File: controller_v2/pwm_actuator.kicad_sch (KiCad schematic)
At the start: 22 parts, among them J1 Conn_01x03_Socket, J2 WAGO 236-402, J3 WAGO 236-402, J4 WAGO 236-404, Q1 2N2222

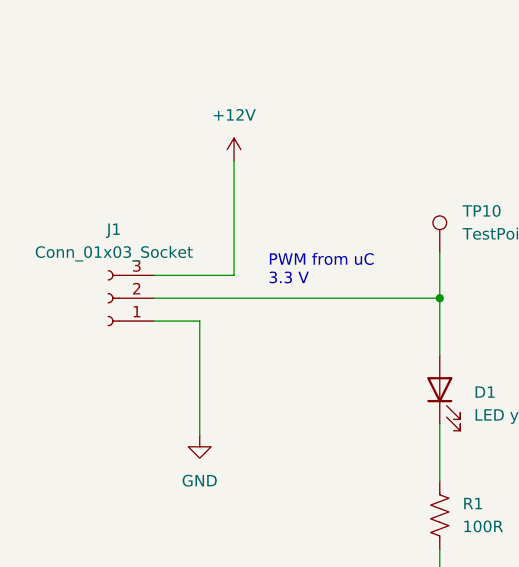
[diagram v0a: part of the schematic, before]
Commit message: Replaced symbols with custom print connector
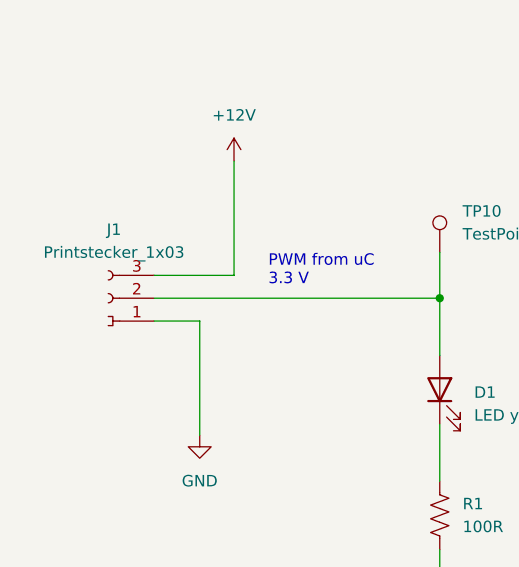
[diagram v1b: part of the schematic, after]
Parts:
- removed J1: Conn_01x03_Socket, Connector_PinSocket_2.54mm:PinSocket_1x03_P2.54mm_Vertical, symbol Connector:Conn_01x03_Socket
- added J1: Printstecker_1x03, connectors:printstecker_1x03_P2.54mm, symbol connectors:printstecker_1x03
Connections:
- net +12V: now also J1.3 (Pin_3)
- net GND: now also J1.1 (Pin_1)
- net at D1.2 (A), TP10.1: now also J1.2 (Pin_2)
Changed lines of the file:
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@@
-    )
-  )
-  (symbol (lib_id "Connector:Conn_01x03_Socket") (at 41.91 88.9 180) (unit 1)
-    (in_bom yes) (on_board yes) (dnp no) (fields_autoplaced)
-    (property "Reference" "J1" (at 42.545 81.28 0)
-      (effects (font (size 1.27 1.27)))
-    )
-    (property "Value" "Conn_01x03_Socket" (at 42.545 83.82 0)
-      (effects (font (size 1.27 1.27)))
-    )
-    (property "Footprint" "Connector_PinSocket_2.54mm:PinSocket_1x03_P2.54mm_Vertical" (at 41.91 88.9 0)
-      (effects (font (size 1.27 1.27)) hide)
-    )
-    (property "Datasheet" "~" (at 41.91 88.9 0)
-      (effects (font (size 1.27 1.27)) hide)
-    )
-    (pin "1")
-    (pin "2")
-    (pin "3")
-    (instances
-      (project "controller"
-        (path "/12246f82-5c9a-456f-a9a1-28ea473855be"
-          (reference "J1") (unit 1)
-        )
-      )
-      (project "controller_v2"
-        (path "/884d8f78-75d7-4449-b027-2ba1bd4eeac8"
-          (reference "J?") (unit 1)
-        )
-        (path "/884d8f78-75d7-4449-b027-2ba1bd4eeac8/e6f5d033-74f5-43d5-8e72-d0169a25c706"
-          (reference "J1") (unit 1)
-        )
-      )
     )
   )
@@
         )
       )
+    )
+  )
+  (symbol (lib_id "connectors:printstecker_1x03") (at 41.91 88.9 180) (unit 1)
+    (in_bom yes) (on_board yes) (dnp no) (fields_autoplaced)
+    (property "Reference" "J1" (at 42.545 81.28 0)
+      (effects (font (size 1.27 1.27)))
+    )
+    (property "Value" "Printstecker_1x03" (at 42.545 83.82 0)
+      (effects (font (size 1.27 1.27)))
+    )
+    (property "Footprint" "connectors:printstecker_1x03_P2.54mm" (at 44.45 80.01 0)
+      (effects (font (size 1.27 1.27)) hide)
+    )
+    (property "Datasheet" "" (at 44.45 88.9 0)
+      (effects (font (size 1.27 1.27)) hide)
+    )
+    (pin "1")
+    (pin "2")
+    (pin "3")
+    (instances
+      (project "controller_v2"
+        (path "/884d8f78-75d7-4449-b027-2ba1bd4eeac8/e6f5d033-74f5-43d5-8e72-d0169a25c706"
+          (reference "J1") (unit 1)
+        )
+      )

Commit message: Cleanup schematic
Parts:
- removed J1: Printstecker_1x03, connectors:printstecker_1x03_P2.54mm, symbol connectors:printstecker_1x03
- removed J4: WAGO 236-404, connectors:WAGO 236-404, symbol connectors:WAGO_236-404
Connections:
- net PWM_FROM_UC: now reaches D1.2 (A), TP10.1
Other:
- note removed: "Debug connector"
- note removed: "Double check diameter, could also be 1.5 (interior)"
